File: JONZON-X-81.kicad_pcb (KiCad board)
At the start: 2 copper layers, 63.5 x 101 mm, 30 parts, among them SW1 SW_DIP_x03, U1 AY-3-8910, U2 74HCT74, U3 74HCT08, U4 74HCT11, U5 74HCT02

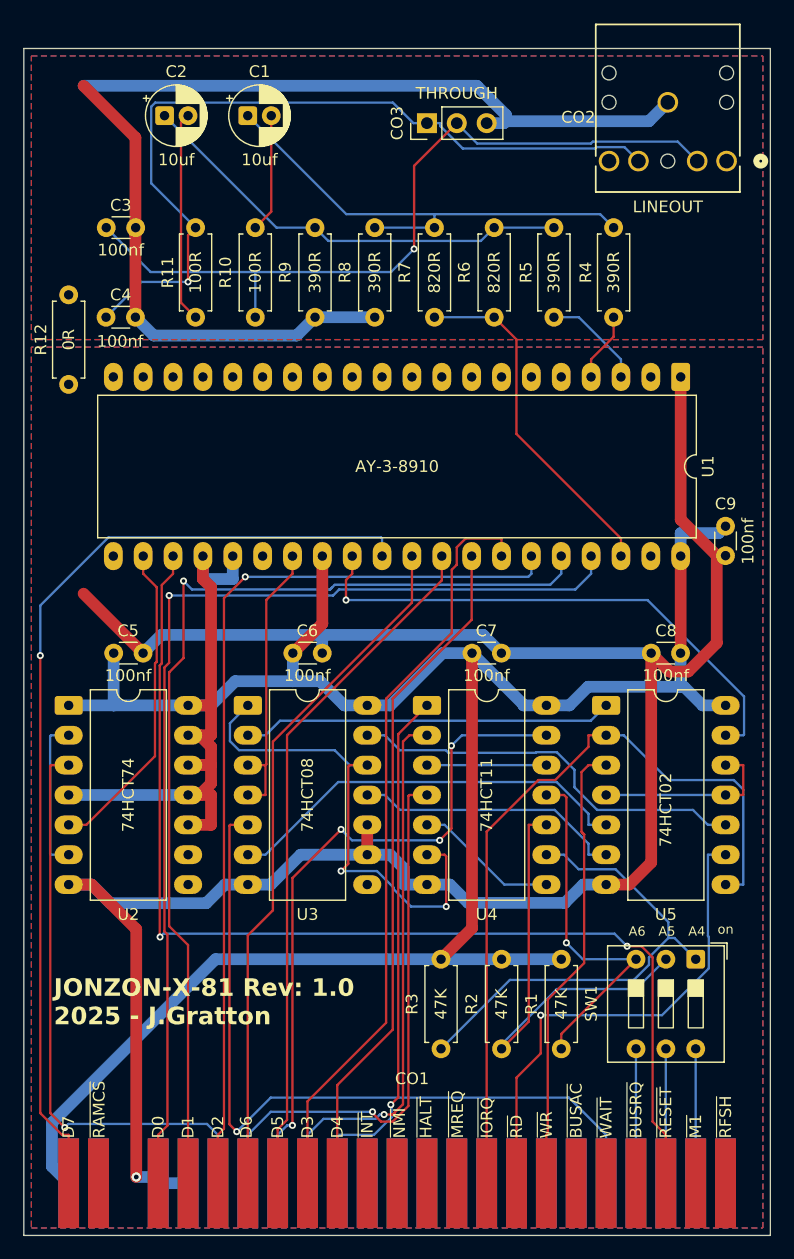
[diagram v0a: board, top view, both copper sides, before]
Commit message: Pulled /A9 low
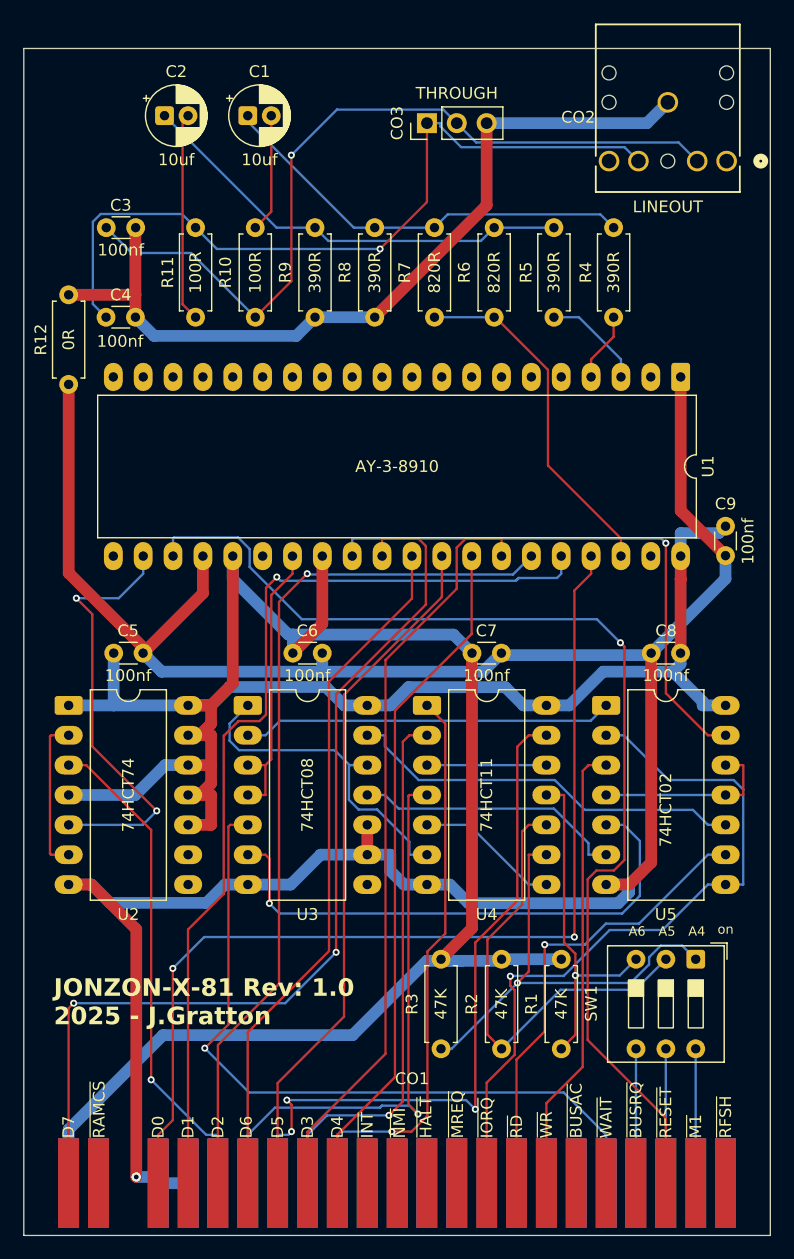
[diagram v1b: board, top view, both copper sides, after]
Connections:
- U1 pad 24: VCC -> GND
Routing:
- net GND: track 194.3 -> 223.3 mm
- net GND_AUDIO: track 97.4 -> 71.6 mm
- net /VALID: track 43.2 -> 28.4 mm, vias 2 -> 0
- net VCC: track 230.1 -> 244.2 mm
- net Net-(U3-Pad6): track 35.1 -> 46.4 mm, vias 0 -> 1
- net /PSGCLK: track 27.3 -> 37.0 mm, vias 0 -> 2
- net /CLK: track 50.5 -> 42.3 mm
- net /D1: track 87.1 -> 82.1 mm
- net Net-(C1-Pad1): track 41.3 -> 36.3 mm
- net /D2: track 78.5 -> 74.7 mm
- net /~{IOREQ}: track 67.2 -> 63.4 mm, vias 0 -> 1
- net /A7: track 65.9 -> 62.7 mm
- net /A3: track 45.7 -> 48.6 mm
- net Net-(CO3-Pin_1): track 68.9 -> 66.4 mm
- net /~{RD}: track 42.3 -> 39.8 mm
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- removed copper zone on B.Cu, net GND
- removed copper zone on F.Cu, net GND
- removed copper zone on B.Cu, net GND_AUDIO
- removed copper zone on F.Cu, net GND_AUDIO

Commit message: updated lots of things
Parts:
- moved C4 47.0 mm to (106.1, 69.2)
- moved C3 47.0 mm to (106.1, 65.4)
- moved R11 7.62 mm to (66.7, 63.5), turned to -90 degrees
- moved C1 1.91 mm to (71.1, 55.9)
- moved C2 1.91 mm to (64.0, 55.9)
- moved C5 1.27 mm to (59.7, 101.0)
- moved C6 1.27 mm to (75.0, 101.0)
- moved C7 1.27 mm to (90.2, 101.0)
- moved C8 1.27 mm to (107.9, 101.0)
- moved R12 0.63 mm to (55.9, 76.2)
- moved C9 0.63 mm to (111.1, 88.9)
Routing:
- net Net-(U3-Pad6): track 46.4 -> 75.3 mm
- net VCC: track 244.2 -> 217.0 mm
- net GND_AUDIO: track 71.6 -> 96.5 mm
- net /~{RESET}: track 95.2 -> 110.4 mm
- net /CLK: track 42.3 -> 55.0 mm, vias 1 -> 2
- net GND: track 223.3 -> 210.7 mm
- net /PSGCLK: track 37.0 -> 26.4 mm, vias 2 -> 0
- net Net-(C2-Pad2): track 17.8 -> 7.89 mm
- net /D7: track 82.8 -> 73.6 mm, vias 2 -> 1
- net /A0: track 49.2 -> 41.6 mm
- net Net-(CO3-Pin_1): track 66.4 -> 73.1 mm, vias 1 -> 0
- net /A1: track 60.0 -> 54.0 mm, vias 3 -> 1
- net /A7: track 62.7 -> 57.9 mm, vias 1 -> 2
- net Net-(R1-Pad2): track 29.7 -> 34.2 mm, vias 1 -> 0
- net /A2: track 47.3 -> 43.2 mm
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- added copper zone on B.Cu, net GND
- added copper zone on F.Cu, net GND
- added copper zone on B.Cu, net GND_AUDIO
- added copper zone on F.Cu, net GND_AUDIO

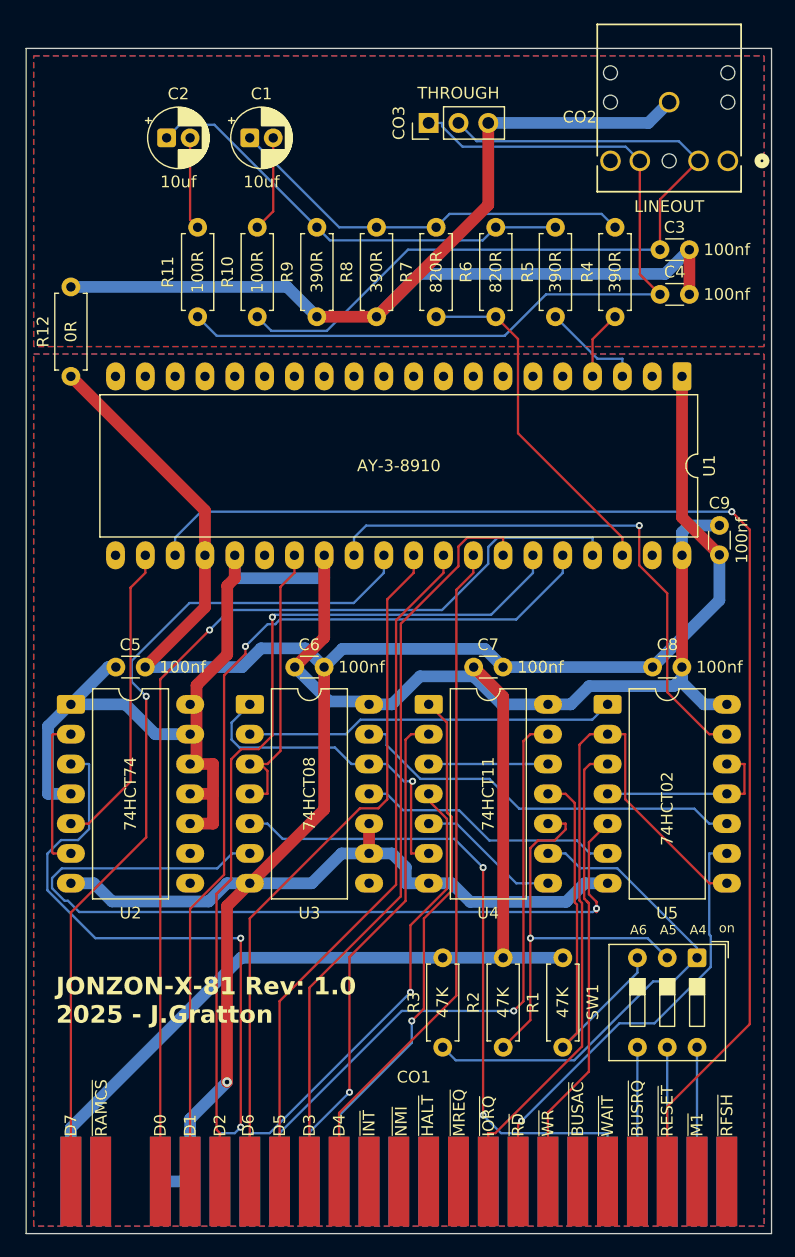
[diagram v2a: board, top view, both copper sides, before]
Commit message: fenced and stiched ground planes
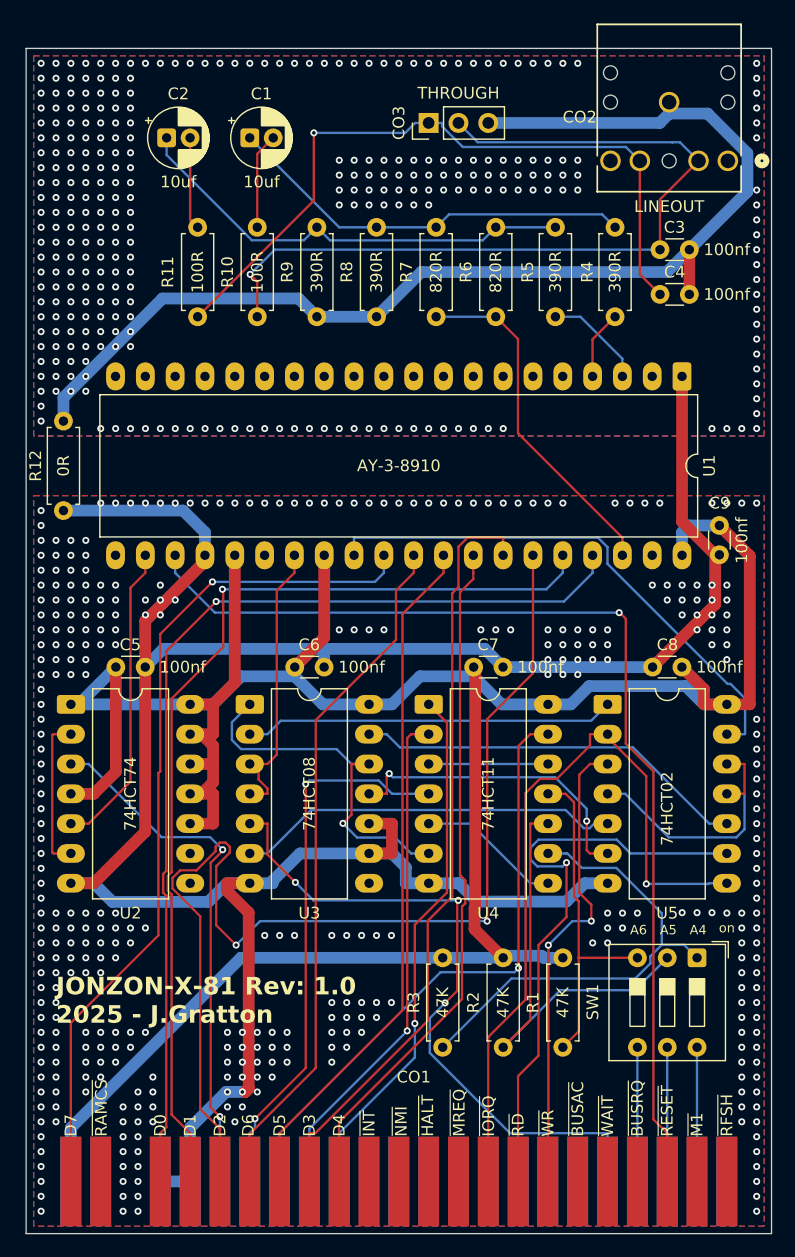
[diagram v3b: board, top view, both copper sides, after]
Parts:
- moved R12 11.4 mm to (55.2, 87.6)
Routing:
- net Net-(U3-Pad6): track 75.3 -> 32.8 mm, vias 1 -> 0
- net /D2: track 76.3 -> 98.6 mm, vias 1 -> 2
- net /~{RESET}: track 110.4 -> 91.0 mm
- net VCC: track 217.0 -> 235.8 mm
- net /~{RD}: track 38.0 -> 50.8 mm
- net Net-(CO3-Pin_1): track 73.1 -> 61.5 mm, vias 0 -> 1
- net /CLK: track 55.0 -> 45.0 mm
- net Net-(U5-Pad11): track 15.7 -> 23.6 mm
- net /D1: track 78.7 -> 84.3 mm
- net GND: track 210.7 -> 216.3 mm, vias 1 -> 361
- net /A0: track 41.6 -> 46.9 mm, vias 1 -> 2
- net Net-(U3-Pad11): track 22.4 -> 27.7 mm, vias 0 -> 2
- net Net-(R1-Pad2): track 34.2 -> 29.4 mm
- net GND_AUDIO: track 96.5 -> 100.7 mm, vias 0 -> 296
- net /VALID: track 28.2 -> 31.4 mm
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
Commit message: removed fab files
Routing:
- net GND_AUDIO: vias 296 -> 316
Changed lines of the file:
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@@
+	)
+	(via
+		(at 97.79 54.61)
+		(size 0.6)
+		(drill 0.3)
+		(layers "F.Cu" "B.Cu")
+		(free yes)
+		(net 93)
 	)
 	(via
@@
 	)
 	(via
+		(at 95.25 52.07)
+		(size 0.6)
+		(drill 0.3)
+		(layers "F.Cu" "B.Cu")
+		(free yes)
+		(net 93)
+	)
+	(via
 		(at 57.15 59.69)
 		(size 0.6)
@@
 	)
 	(via
+		(at 97.79 52.07)
+		(size 0.6)
+		(drill 0.3)
+		(layers "F.Cu" "B.Cu")
+		(free yes)
+		(net 93)
+	)
+	(via
 		(at 71.12 80.645)
 		(size 0.6)
@@
 	)
 	(via
+		(at 97.79 53.34)
+		(size 0.6)
+		(drill 0.3)
+		(layers "F.Cu" "B.Cu")
+		(free yes)
+		(net 93)
+	)
+	(via
 		(at 64.77 49.53)
 		(size 0.6)
@@
 	)
 	(via
+		(at 95.25 54.61)
+		(size 0.6)
+		(drill 0.3)
+		(layers "F.Cu" "B.Cu")
+		(free yes)
+		(net 93)
+	)
+	(via
 		(at 58.42 69.85)
 		(size 0.6)
@@
 	)
 	(via
+		(at 93.98 50.8)
+		(size 0.6)
+		(drill 0.3)
+		(layers "F.Cu" "B.Cu")
+		(free yes)
+		(net 93)
+	)
+	(via
 		(at 83.82 60.325)
 		(size 0.6)
@@
 	)
 	(via
+		(at 93.98 53.34)
+		(size 0.6)
+		(drill 0.3)
+		(layers "F.Cu" "B.Cu")
+		(free yes)
+		(net 93)
+	)
+	(via
 		(at 60.96 49.53)
 		(size 0.6)
@@
 	)
 	(via
+		(at 97.79 50.8)
+		(size 0.6)
+		(drill 0.3)
+		(layers "F.Cu" "B.Cu")
+		(free yes)
+		(net 93)
+	)
+	(via
 		(at 60.96 57.15)
 		(size 0.6)
@@
 	)
 	(via
+		(at 95.25 53.34)
+		(size 0.6)
+		(drill 0.3)
+		(layers "F.Cu" "B.Cu")
+		(free yes)
+		(net 93)
+	)
+	(via
 		(at 72.39 49.53)
 		(size 0.6)
@@
 	)
 	(via
+		(at 96.52 54.61)
+		(size 0.6)
+		(drill 0.3)
+		(layers "F.Cu" "B.Cu")
+		(free yes)
+		(net 93)
+	)
+	(via
 		(at 62.23 80.645)
 		(size 0.6)
@@
 	)
 	(via
+		(at 96.52 52.07)
+		(size 0.6)
+		(drill 0.3)
+		(layers "F.Cu" "B.Cu")
+		(free yes)
+		(net 93)
+	)
+	(via
 		(at 60.96 53.34)
 		(size 0.6)
@@
 	)
 	(via
+		(at 99.06 52.07)
+		(size 0.6)
+		(drill 0.3)
+		(layers "F.Cu" "B.Cu")
+		(free yes)
+		(net 93)
+	)
+	(via
 		(at 114.3 53.34)
 		(size 0.6)
@@
 	)
 	(via
+		(at 93.98 54.61)
+		(size 0.6)
+		(drill 0.3)
+		(layers "F.Cu" "B.Cu")
+		(free yes)
+		(net 93)
+	)
+	(via
 		(at 76.2 80.645)
 		(size 0.6)
@@
 	)
 	(via
+		(at 93.98 52.07)
+		(size 0.6)
+		(drill 0.3)
+		(layers "F.Cu" "B.Cu")
+		(free yes)
+		(net 93)
+	)
+	(via
 		(at 59.69 49.53)
 		(size 0.6)
@@
 	)
 	(via
+		(at 96.52 53.34)
+		(size 0.6)
+		(drill 0.3)
+		(layers "F.Cu" "B.Cu")
+		(free yes)
+		(net 93)
+	)
+	(via
 		(at 58.42 59.69)
 		(size 0.6)
@@
 	)
 	(via
+		(at 95.25 50.8)
+		(size 0.6)
+		(drill 0.3)
+		(layers "F.Cu" "B.Cu")
+		(free yes)
+		(net 93)
+	)
+	(via
 		(at 78.74 61.595)
 		(size 0.6)
@@
 	)
 	(via
+		(at 99.06 54.61)
+		(size 0.6)
+		(drill 0.3)
+		(layers "F.Cu" "B.Cu")
+		(free yes)
+		(net 93)
+	)
+	(via
 		(at 57.15 57.15)
 		(size 0.6)
@@
 	)
 	(via
+		(at 96.52 50.8)
+		(size 0.6)
+		(drill 0.3)
+		(layers "F.Cu" "B.Cu")
+		(free yes)
+		(net 93)
+	)
+	(via
 		(at 114.3 78.105)
 		(size 0.6)
@@
 	)
 	(via
+		(at 99.06 50.8)
+		(size 0.6)
+		(drill 0.3)
+		(layers "F.Cu" "B.Cu")
+		(free yes)
+		(net 93)
+	)
+	(via
 		(at 62.23 49.53)
 		(size 0.6)
@@
 		(size 0.6)
 		(drill 0.3)
+		(layers "F.Cu" "B.Cu")
+		(free yes)
+		(net 93)
+	)
+	(via
+		(at 99.06 53.34)
+		(size 0.6)
+		(drill 0.3)

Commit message: corrected connections on audio jack as the footprint does not match the schematic symbol pinout. the left and right where on rev 1.0 connected to shunts a and b. to correct this I will just place shorts between pins 3 and 4 and 1 and 2 when the rev 1.0 boards arrive.
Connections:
- CO2 pad 1: unconnected-(CO2-Pad1) -> Net-(CO3-Pin_2)
- CO2 pad 2: Net-(CO3-Pin_2) -> unconnected-(CO2-Pad2)
- CO2 pad 3: Net-(CO3-Pin_1) -> unconnected-(CO2-Pad3)
- CO2 pad 4: unconnected-(CO2-Pad4) -> Net-(CO3-Pin_1)
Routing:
- net Net-(CO3-Pin_2): track 70.4 -> 73.9 mm
- net Net-(CO3-Pin_1): track 61.5 -> 59.8 mm
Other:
- board text added: "JONZON-X-81 Rev: 1.1 2025 - J.Gratton"
- board text removed: "JONZON-X-81 Rev: 1.0 2025 - J.Gratton"
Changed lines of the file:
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@@
 		(title "JONZON-X-81")
 		(date "2025-08-11")
-		(rev "1.0")
+		(rev "1.1")
 	)
 	(layers
@@
 	(net 80 "unconnected-(CO1-~{NMI}-PadB14)")
 	(net 81 "unconnected-(CO1-~{RFSH}-PadB25)")
-	(net 82 "unconnected-(CO2-Pad4)")
+	(net 82 "unconnected-(CO2-Pad2)")
 	(net 83 "unconnected-(U2B-~{Q}-Pad8)")
 	(net 84 "unconnected-(U2B-Q-Pad9)")
@@
 	(net 90 "Net-(U4-Pad5)")
 	(net 91 "Net-(U5-Pad11)")
-	(net 92 "unconnected-(CO2-Pad1)")
+	(net 92 "unconnected-(CO2-Pad3)")
 	(net 93 "GND_AUDIO")
 	(footprint "Capacitor_THT:C_Disc_D3.0mm_W1.6mm_P2.50mm"
@@
 			(layers "*.Cu" "*.Mask")
 			(remove_unused_layers no)
-			(net 92 "unconnected-(CO2-Pad1)")
+			(net 10 "Net-(CO3-Pin_2)")
 			(pinfunction "1")
-			(pintype "unspecified+no_connect")
+			(pintype "unspecified")
 		)
 		(pad "2" thru_hole circle
@@
 			(layers "*.Cu" "*.Mask")
 			(remove_unused_layers no)
-			(net 10 "Net-(CO3-Pin_2)")
+			(net 82 "unconnected-(CO2-Pad2)")
 			(pinfunction "2")
-			(pintype "unspecified")
+			(pintype "unspecified+no_connect")
 		)
 		(pad "3" thru_hole circle
@@
 			(layers "*.Cu" "*.Mask")
 			(remove_unused_layers no)
-			(net 12 "Net-(CO3-Pin_1)")
+			(net 92 "unconnected-(CO2-Pad3)")
 			(pinfunction "3")
-			(pintype "unspecified")
+			(pintype "unspecified+no_connect")
 		)
 		(pad "4" thru_hole circle
@@
 			(layers "*.Cu" "*.Mask")
 			(remove_unused_layers no)
-			(net 82 "unconnected-(CO2-Pad4)")
+			(net 12 "Net-(CO3-Pin_1)")
 			(pinfunction "4")
-			(pintype "unspecified+no_connect")
+			(pintype "unspecified")
 		)
 		(pad "5" thru_hole circle
@@
 		(layer "Edge.Cuts")
 	)
-	(gr_text "JONZON-X-81 Rev: 1.0\n2025 - J.Gratton"
+	(gr_text "JONZON-X-81 Rev: 1.1\n2025 - J.Gratton"
 		(at 54.61 131.445 0)
 		(layer "F.SilkS")
@@
 	)
 	(segment
-		(start 106.065 65.405)
-		(end 106.065 61.1201)
+		(start 106.065 64.155)
+		(end 106.065 65.405)
 		(width 0.2)
 		(layer "F.Cu")
@@
 	)
 	(segment
-		(start 106.065 61.1201)
-		(end 109.3451 57.84)
+		(start 106.045 63.6401)
+		(end 106.045 64.135)
+		(width 0.2)
+		(layer "F.Cu")
+		(net 10)
+	)
+	(segment
+		(start 106.045 64.135)
+		(end 106.065 64.155)
+		(width 0.2)
+		(layer "F.Cu")
+		(net 10)
+	)
+	(segment
+		(start 111.8451 57.84)
+		(end 106.045 63.6401)
 		(width 0.2)
 		(layer "F.Cu")
@@
 	)
 	(segment
-		(start 107.7621 56.257)
-		(end 109.3451 57.84)
+		(start 110.2621 56.257)
+		(end 111.8451 57.84)
 		(width 0.2)
 		(layer "B.Cu")
@@
 	)
 	(segment
-		(start 90.5405 56.2555)
-		(end 107.1123 56.2555)
-		(width 0.2)
-		(layer "B.Cu")
-		(net 10)
-	)
-	(segment
-		(start 107.1138 56.257)
-		(end 107.7621 56.257)
+		(start 88.895 54.61)
+		(end 90.5405 56.2555)
 		(width 0.2)
 		(layer "B.Cu")
@@
 	)
 	(segment
-		(start 88.895 54.61)
-		(end 90.5405 56.2555)
+		(start 90.5405 56.2555)
+		(end 107.1123 56.2555)
 		(width 0.2)
 		(layer "B.Cu")
@@
 	)
 	(segment
+		(start 107.1138 56.257)
+		(end 110.2621 56.257)
+		(width 0.2)
+		(layer "B.Cu")
+		(net 10)
+	)
+	(segment
 		(start 73.655 144.78)
 		(end 73.655 140.6683)
@@
 	)
 	(segment
-		(start 66.675 71.12)
-		(end 76.5768 61.2182)
+		(start 101.8451 57.84)
+		(end 104.14 60.1349)
+		(width 0.2)
+		(layer "F.Cu")
+		(net 12)
+	)
+	(segment
+		(start 104.14 67.29)
+		(end 106.065 69.215)
 		(width 0.2)
 		(layer "F.Cu")
@@
 	)
 	(segment
-		(start 104.3451 67.4951)
-		(end 104.3451 57.84)
+		(start 66.675 71.12)
+		(end 76.5768 61.2182)
 		(width 0.2)
 		(layer "F.Cu")
@@
 	)
 	(segment
-		(start 106.065 69.215)
-		(end 104.3451 67.4951)
+		(start 104.14 60.1349)
+		(end 104.14 67.29)
 		(width 0.2)
 		(layer "F.Cu")
@@
 	)
 	(segment
-		(start 86.355 54.61)
-		(end 85.2033 54.61)
-		(width 0.2)
-		(layer "B.Cu")
-		(net 12)
-	)
-	(segment
-		(start 87.5067 54.8979)
-		(end 87.5067 54.61)
+		(start 86.995 54.61)
+		(end 89.0415 56.6565)
 		(width 0.2)
 		(layer "B.Cu")
@@
 	(segment
 		(start 86.355 54.61)
-		(end 87.5067 54.61)
+		(end 85.2033 54.61)
 		(width 0.2)
 		(layer "B.Cu")
@@
 	)
 	(segment
-		(start 89.2661 56.6573)
-		(end 87.5067 54.8979)
+		(start 86.355 54.61)
+		(end 86.995 54.61)
 		(width 0.2)
 		(layer "B.Cu")
@@
 	)
 	(segment
-		(start 103.1624 56.6573)
-		(end 89.2661 56.6573)
+		(start 100.6616 56.6565)
+		(end 101.8451 57.84)
 		(width 0.2)
 		(layer "B.Cu")
@@
 	)
 	(segment
-		(start 104.3451 57.84)
-		(end 103.1624 56.6573)
+		(start 89.0415 56.6565)
+		(end 100.6616 56.6565)
 		(width 0.2)
 		(layer "B.Cu")

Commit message: commented rev 1.1 on the PCB
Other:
- board text added: "Rev: 1.1 was a change to the Audio Jack connections. Left and Right where connected to the Shunts."
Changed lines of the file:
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@@
 		(layer "Edge.Cuts")
+	)
+	(gr_text "Rev: 1.1 was a change to the Audio Jack connections.\nLeft and Right where connected to the Shunts."
+		(at 177.8 171.45 0)
+		(layer "F.Cu")
+		(effects
+			(font
+				(size 1.5 1.5)
+				(thickness 0.2)
+			)
+			(justify left bottom)
+		)
 	)
 	(gr_text "JONZON-X-81 Rev: 1.1\n2025 - J.Gratton"

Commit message: updated rev 1.1 and readme.
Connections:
- R4 pad 1: /OUTA -> /OUTB
- R5 pad 1: /OUTB -> /OUTA
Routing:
- net /OUTB: track 8.69 -> 5.34 mm
- net /OUTA: track 5.87 -> 6.39 mm
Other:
- board text added: "Rev: 1.1 was a change to the Audio Jack connections. Left and Right where connected to Shunts A and B. This also resulted in a Left and Right swap, so Channel A and B where reveresed to compensate."
- board text removed: "Rev: 1.1 was a change to the Audio Jack connections. Left and Right where connected to the Shunts."
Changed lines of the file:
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@@
 			(layers "*.Cu" "*.Mask")
 			(remove_unused_layers no)
-			(net 52 "/OUTA")
+			(net 51 "/OUTB")
 			(pintype "passive")
 		)
@@
 			(layers "*.Cu" "*.Mask")
 			(remove_unused_layers no)
-			(net 51 "/OUTB")
+			(net 52 "/OUTA")
 			(pintype "passive")
 		)
@@
 		(layer "Edge.Cuts")
 	)
-	(gr_text "Rev: 1.1 was a change to the Audio Jack connections.\nLeft and Right where connected to the Shunts."
+	(gr_text "Rev: 1.1 was a change to the Audio Jack connections.\nLeft and Right where connected to Shunts A and B.\nThis also resulted in a Left and Right swap, so Channel A and B where reveresed to compensate."
 		(at 177.8 171.45 0)
 		(layer "F.Cu")
 		(effects
 			(font
-				(size 1.5 1.5)
+				(size 1 1)
 				(thickness 0.2)
 			)
@@
 	)
 	(segment
-		(start 97.155 71.12)
-		(end 99.2817 71.12)
+		(start 102.235 71.12)
+		(end 102.86 71.745)
 		(width 0.2)
 		(layer "B.Cu")
@@
 	(segment
 		(start 102.86 76.2)
-		(end 102.86 74.6983)
-		(width 0.2)
-		(layer "B.Cu")
-		(net 51)
-	)
-	(segment
-		(start 99.2817 71.12)
-		(end 102.86 74.6983)
+		(end 102.86 71.745)
 		(width 0.2)
 		(layer "B.Cu")
@@
 	)
 	(segment
-		(start 100.32 76.2)
-		(end 100.32 73.035)
+		(start 100.32 74.285)
+		(end 97.155 71.12)
 		(width 0.2)
 		(layer "F.Cu")
@@
 	)
 	(segment
-		(start 100.32 73.035)
-		(end 102.235 71.12)
+		(start 100.32 76.2)
+		(end 100.32 74.285)
 		(width 0.2)
 		(layer "F.Cu")
